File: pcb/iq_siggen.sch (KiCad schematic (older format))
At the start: 130 parts, among them J1 Conn_Coaxial, J10 Conn_01x01_Male, J11 Conn_01x01_Male, J12 Conn_01x01_Male, J13 Conn_01x01_Male, J14 Conn_01x01_Male, J15 Conn_Coaxial, J16 Conn_Coaxial, J17 Conn_01x01_Male, J2 Barrel_Jack_MountingPin, J3 J3 - BANK0, J4 J4 - BANK1, J5 Conn_Coaxial, J6 Conn_Coaxial, J7 Conn_01x10_Male, J8 Conn_01x01_Male, J9 Conn_01x10_Male, SW1 SW_Push, SW2 SW_Push, SW3 SW_Push, SW4 SW_Push, U1 AMS1117-3.3, U2 TPS72325DBVR, U3 TLV73325PDBVT

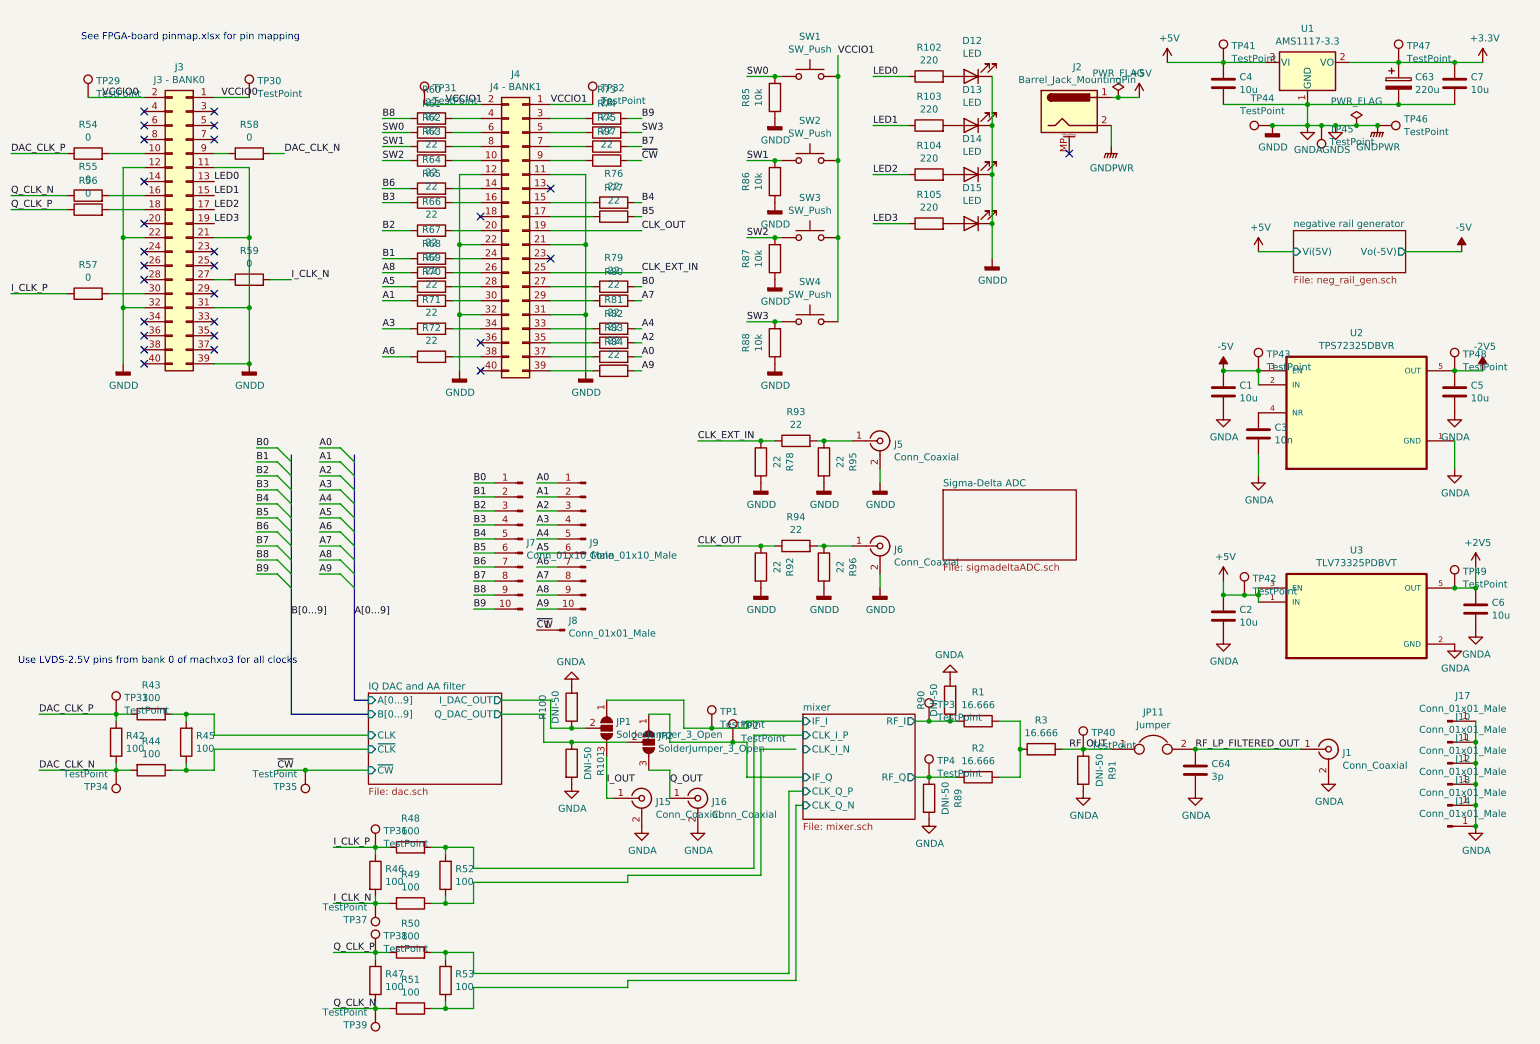
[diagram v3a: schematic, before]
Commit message: Update footprints, move to 0603 passives for JLCPCB assembly, create transformer footprints
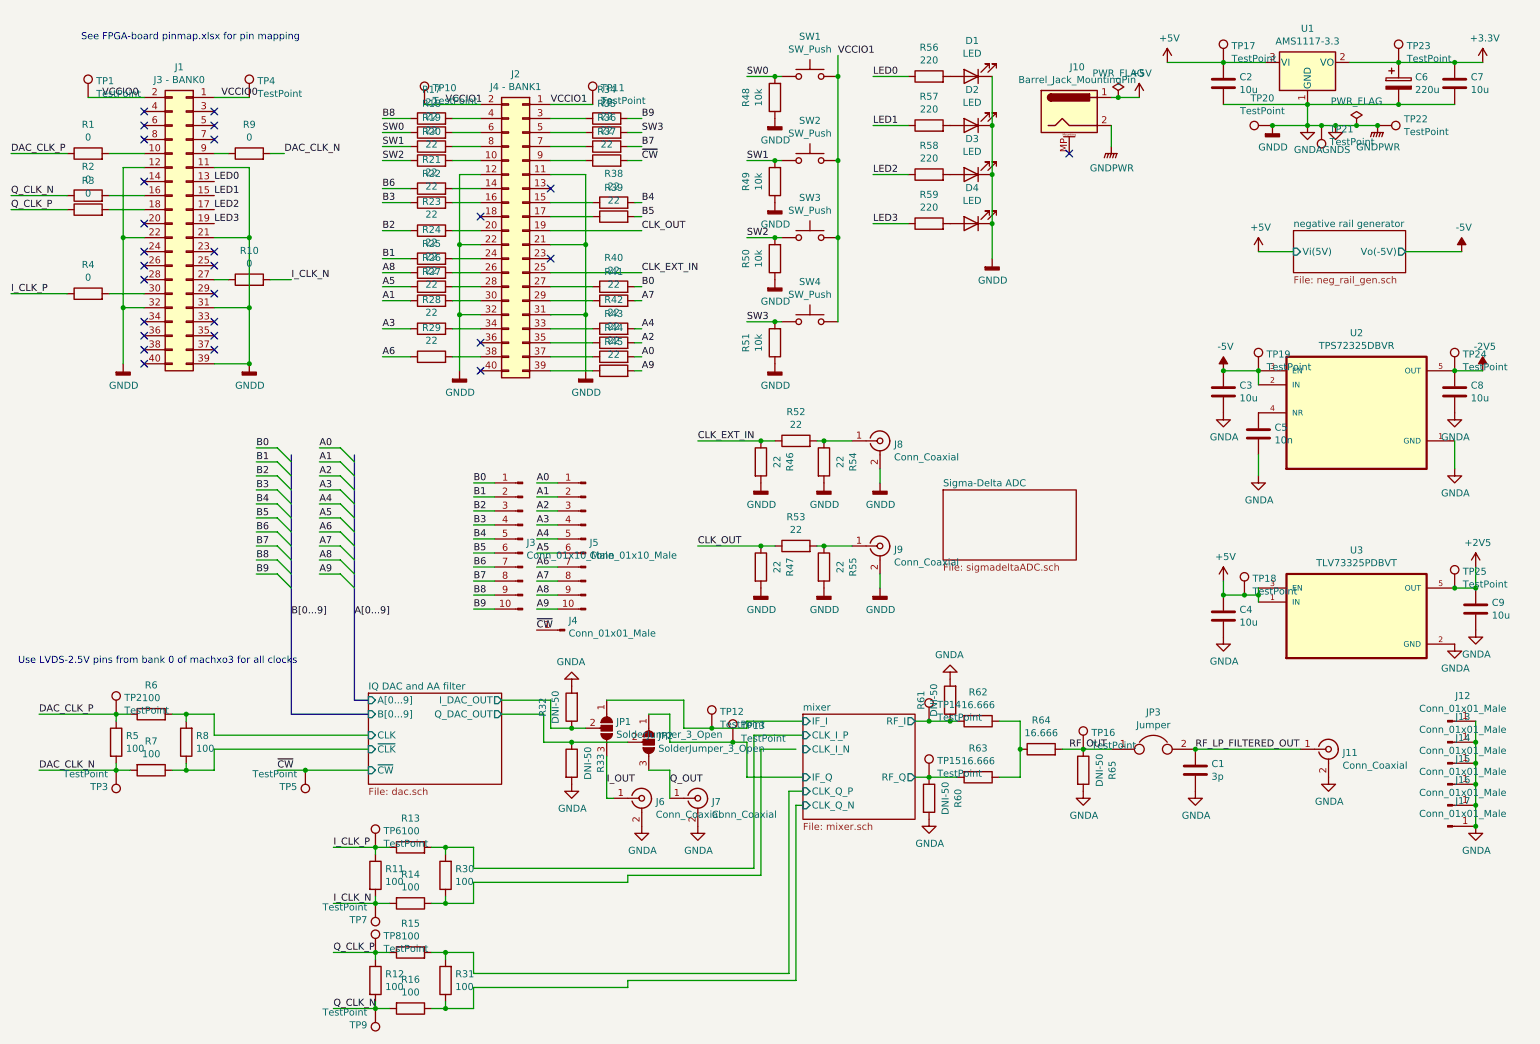
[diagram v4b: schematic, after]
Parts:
- C1: renamed from C64; footprint Capacitor_SMD:C_0805_2012Metric_Pad1.15x1.40mm_HandSolder -> Capacitor_SMD:C_0603_1608Metric
- C2: renamed from C4; footprint Capacitor_SMD:C_0805_2012Metric_Pad1.15x1.40mm_HandSolder -> Capacitor_SMD:C_0603_1608Metric
- C3: renamed from C1; footprint Capacitor_SMD:C_0805_2012Metric_Pad1.15x1.40mm_HandSolder -> Capacitor_SMD:C_0603_1608Metric
- C4: renamed from C2; footprint Capacitor_SMD:C_0805_2012Metric_Pad1.15x1.40mm_HandSolder -> Capacitor_SMD:C_0603_1608Metric
- C5: renamed from C3; footprint Capacitor_SMD:C_0805_2012Metric_Pad1.15x1.40mm_HandSolder -> Capacitor_SMD:C_0603_1608Metric
- C7: footprint Capacitor_SMD:C_0805_2012Metric_Pad1.15x1.40mm_HandSolder -> Capacitor_SMD:C_0603_1608Metric
- C8: renamed from C5; footprint Capacitor_SMD:C_0805_2012Metric_Pad1.15x1.40mm_HandSolder -> Capacitor_SMD:C_0603_1608Metric
- C9: renamed from C6; footprint Capacitor_SMD:C_0805_2012Metric_Pad1.15x1.40mm_HandSolder -> Capacitor_SMD:C_0603_1608Metric
- J1: renamed from J3; footprint (none) -> Connector_PinHeader_2.54mm:PinHeader_2x20_P2.54mm_Vertical
- J11: renamed from J1; footprint (none) -> Connector_Coaxial:SMA_Amphenol_132289_EdgeMount
- J12: renamed from J17; footprint (none) -> Connector_PinHeader_2.54mm:PinHeader_1x01_P2.54mm_Vertical
- J13: renamed from J10; footprint (none) -> Connector_PinHeader_2.54mm:PinHeader_1x01_P2.54mm_Vertical
- J14: renamed from J11; footprint (none) -> Connector_PinHeader_2.54mm:PinHeader_1x01_P2.54mm_Vertical
- J15: renamed from J12; footprint (none) -> Connector_PinHeader_2.54mm:PinHeader_1x01_P2.54mm_Vertical
- J16: renamed from J13; footprint (none) -> Connector_PinHeader_2.54mm:PinHeader_1x01_P2.54mm_Vertical
- J17: renamed from J14; footprint (none) -> Connector_PinHeader_2.54mm:PinHeader_1x01_P2.54mm_Vertical
- J2: renamed from J4; footprint (none) -> Connector_PinHeader_2.54mm:PinHeader_2x20_P2.54mm_Vertical
- J3: renamed from J7; footprint (none) -> Connector_PinHeader_2.54mm:PinHeader_1x10_P2.54mm_Vertical
- J4: renamed from J8; footprint (none) -> Connector_PinHeader_2.54mm:PinHeader_1x01_P2.54mm_Vertical
- J5: renamed from J9; footprint (none) -> Connector_PinHeader_2.54mm:PinHeader_1x10_P2.54mm_Vertical
- J6: renamed from J15; footprint (none) -> Connector_Coaxial:SMA_Amphenol_132289_EdgeMount
- J7: renamed from J16; footprint (none) -> Connector_Coaxial:SMA_Amphenol_132289_EdgeMount
- J8: renamed from J5; footprint (none) -> Connector_Coaxial:SMA_Amphenol_132289_EdgeMount
- J9: renamed from J6; footprint (none) -> Connector_Coaxial:SMA_Amphenol_132289_EdgeMount
- R1: renamed from R54; footprint Resistor_SMD:R_0805_2012Metric_Pad1.20x1.40mm_HandSolder -> Resistor_SMD:R_0603_1608Metric
- R10: renamed from R59; footprint Resistor_SMD:R_0805_2012Metric_Pad1.20x1.40mm_HandSolder -> Resistor_SMD:R_0603_1608Metric
- R11: renamed from R46; footprint Resistor_SMD:R_0805_2012Metric_Pad1.20x1.40mm_HandSolder -> Resistor_SMD:R_0603_1608Metric
- R12: renamed from R47; footprint Resistor_SMD:R_0805_2012Metric_Pad1.20x1.40mm_HandSolder -> Resistor_SMD:R_0603_1608Metric
- R13: renamed from R48; footprint Resistor_SMD:R_0805_2012Metric_Pad1.20x1.40mm_HandSolder -> Resistor_SMD:R_0603_1608Metric
- R14: renamed from R49; footprint Resistor_SMD:R_0805_2012Metric_Pad1.20x1.40mm_HandSolder -> Resistor_SMD:R_0603_1608Metric
- R15: renamed from R50; footprint Resistor_SMD:R_0805_2012Metric_Pad1.20x1.40mm_HandSolder -> Resistor_SMD:R_0603_1608Metric
- R16: renamed from R51; footprint Resistor_SMD:R_0805_2012Metric_Pad1.20x1.40mm_HandSolder -> Resistor_SMD:R_0603_1608Metric
- R17: renamed from R60; footprint Resistor_SMD:R_0805_2012Metric_Pad1.20x1.40mm_HandSolder -> Resistor_SMD:R_0603_1608Metric
- R18: renamed from R61; footprint Resistor_SMD:R_0805_2012Metric_Pad1.20x1.40mm_HandSolder -> Resistor_SMD:R_0603_1608Metric
- R19: renamed from R62; footprint Resistor_SMD:R_0805_2012Metric_Pad1.20x1.40mm_HandSolder -> Resistor_SMD:R_0603_1608Metric
- R2: renamed from R55; footprint Resistor_SMD:R_0805_2012Metric_Pad1.20x1.40mm_HandSolder -> Resistor_SMD:R_0603_1608Metric
- R20: renamed from R63; footprint Resistor_SMD:R_0805_2012Metric_Pad1.20x1.40mm_HandSolder -> Resistor_SMD:R_0603_1608Metric
- R21: renamed from R64; footprint Resistor_SMD:R_0805_2012Metric_Pad1.20x1.40mm_HandSolder -> Resistor_SMD:R_0603_1608Metric
- R22: renamed from R65; footprint Resistor_SMD:R_0805_2012Metric_Pad1.20x1.40mm_HandSolder -> Resistor_SMD:R_0603_1608Metric
- R23: renamed from R66; footprint Resistor_SMD:R_0805_2012Metric_Pad1.20x1.40mm_HandSolder -> Resistor_SMD:R_0603_1608Metric
- R24: renamed from R67; footprint Resistor_SMD:R_0805_2012Metric_Pad1.20x1.40mm_HandSolder -> Resistor_SMD:R_0603_1608Metric
- R25: renamed from R68; footprint Resistor_SMD:R_0805_2012Metric_Pad1.20x1.40mm_HandSolder -> Resistor_SMD:R_0603_1608Metric
- R26: renamed from R69; footprint Resistor_SMD:R_0805_2012Metric_Pad1.20x1.40mm_HandSolder -> Resistor_SMD:R_0603_1608Metric
- R27: renamed from R70; footprint Resistor_SMD:R_0805_2012Metric_Pad1.20x1.40mm_HandSolder -> Resistor_SMD:R_0603_1608Metric
- R28: renamed from R71; footprint Resistor_SMD:R_0805_2012Metric_Pad1.20x1.40mm_HandSolder -> Resistor_SMD:R_0603_1608Metric
- R29: renamed from R72; footprint Resistor_SMD:R_0805_2012Metric_Pad1.20x1.40mm_HandSolder -> Resistor_SMD:R_0603_1608Metric
- R3: renamed from R56; footprint Resistor_SMD:R_0805_2012Metric_Pad1.20x1.40mm_HandSolder -> Resistor_SMD:R_0603_1608Metric
- R30: renamed from R52; footprint Resistor_SMD:R_0805_2012Metric_Pad1.20x1.40mm_HandSolder -> Resistor_SMD:R_0603_1608Metric
- R31: renamed from R53; footprint Resistor_SMD:R_0805_2012Metric_Pad1.20x1.40mm_HandSolder -> Resistor_SMD:R_0603_1608Metric
- R32: renamed from R100; footprint Resistor_SMD:R_0805_2012Metric_Pad1.20x1.40mm_HandSolder -> Resistor_SMD:R_0603_1608Metric
- R33: renamed from R101; footprint Resistor_SMD:R_0805_2012Metric_Pad1.20x1.40mm_HandSolder -> Resistor_SMD:R_0603_1608Metric
- R34: renamed from R73; footprint Resistor_SMD:R_0805_2012Metric_Pad1.20x1.40mm_HandSolder -> Resistor_SMD:R_0603_1608Metric
- R35: renamed from R74; footprint Resistor_SMD:R_0805_2012Metric_Pad1.20x1.40mm_HandSolder -> Resistor_SMD:R_0603_1608Metric
- R36: renamed from R75; footprint Resistor_SMD:R_0805_2012Metric_Pad1.20x1.40mm_HandSolder -> Resistor_SMD:R_0603_1608Metric
- R37: renamed from R97; footprint Resistor_SMD:R_0805_2012Metric_Pad1.20x1.40mm_HandSolder -> Resistor_SMD:R_0603_1608Metric
- R38: renamed from R76; footprint Resistor_SMD:R_0805_2012Metric_Pad1.20x1.40mm_HandSolder -> Resistor_SMD:R_0603_1608Metric
- R39: renamed from R77; footprint Resistor_SMD:R_0805_2012Metric_Pad1.20x1.40mm_HandSolder -> Resistor_SMD:R_0603_1608Metric
- R4: renamed from R57; footprint Resistor_SMD:R_0805_2012Metric_Pad1.20x1.40mm_HandSolder -> Resistor_SMD:R_0603_1608Metric
- R40: renamed from R79; footprint Resistor_SMD:R_0805_2012Metric_Pad1.20x1.40mm_HandSolder -> Resistor_SMD:R_0603_1608Metric
- R41: renamed from R80; footprint Resistor_SMD:R_0805_2012Metric_Pad1.20x1.40mm_HandSolder -> Resistor_SMD:R_0603_1608Metric
- R42: renamed from R81; footprint Resistor_SMD:R_0805_2012Metric_Pad1.20x1.40mm_HandSolder -> Resistor_SMD:R_0603_1608Metric
- R43: renamed from R82; footprint Resistor_SMD:R_0805_2012Metric_Pad1.20x1.40mm_HandSolder -> Resistor_SMD:R_0603_1608Metric
- R44: renamed from R83; footprint Resistor_SMD:R_0805_2012Metric_Pad1.20x1.40mm_HandSolder -> Resistor_SMD:R_0603_1608Metric
- R45: renamed from R84; footprint Resistor_SMD:R_0805_2012Metric_Pad1.20x1.40mm_HandSolder -> Resistor_SMD:R_0603_1608Metric
- R46: renamed from R78; footprint Resistor_SMD:R_0805_2012Metric_Pad1.20x1.40mm_HandSolder -> Resistor_SMD:R_0603_1608Metric
- R47: renamed from R92; footprint Resistor_SMD:R_0805_2012Metric_Pad1.20x1.40mm_HandSolder -> Resistor_SMD:R_0603_1608Metric
- R48: renamed from R85; footprint Resistor_SMD:R_0805_2012Metric_Pad1.20x1.40mm_HandSolder -> Resistor_SMD:R_0603_1608Metric
- R49: renamed from R86; footprint Resistor_SMD:R_0805_2012Metric_Pad1.20x1.40mm_HandSolder -> Resistor_SMD:R_0603_1608Metric
- R5: renamed from R42; footprint Resistor_SMD:R_0805_2012Metric_Pad1.20x1.40mm_HandSolder -> Resistor_SMD:R_0603_1608Metric
- R50: renamed from R87; footprint Resistor_SMD:R_0805_2012Metric_Pad1.20x1.40mm_HandSolder -> Resistor_SMD:R_0603_1608Metric
- R51: renamed from R88; footprint Resistor_SMD:R_0805_2012Metric_Pad1.20x1.40mm_HandSolder -> Resistor_SMD:R_0603_1608Metric
- R52: renamed from R93; footprint Resistor_SMD:R_0805_2012Metric_Pad1.20x1.40mm_HandSolder -> Resistor_SMD:R_0603_1608Metric
- R53: renamed from R94; footprint Resistor_SMD:R_0805_2012Metric_Pad1.20x1.40mm_HandSolder -> Resistor_SMD:R_0603_1608Metric
- R54: renamed from R95; footprint Resistor_SMD:R_0805_2012Metric_Pad1.20x1.40mm_HandSolder -> Resistor_SMD:R_0603_1608Metric
- R55: renamed from R96; footprint Resistor_SMD:R_0805_2012Metric_Pad1.20x1.40mm_HandSolder -> Resistor_SMD:R_0603_1608Metric
- R56: renamed from R102; footprint Resistor_SMD:R_0805_2012Metric_Pad1.20x1.40mm_HandSolder -> Resistor_SMD:R_0603_1608Metric
- R57: renamed from R103; footprint Resistor_SMD:R_0805_2012Metric_Pad1.20x1.40mm_HandSolder -> Resistor_SMD:R_0603_1608Metric
- R58: renamed from R104; footprint Resistor_SMD:R_0805_2012Metric_Pad1.20x1.40mm_HandSolder -> Resistor_SMD:R_0603_1608Metric
- R59: renamed from R105; footprint Resistor_SMD:R_0805_2012Metric_Pad1.20x1.40mm_HandSolder -> Resistor_SMD:R_0603_1608Metric
- R6: renamed from R43; footprint Resistor_SMD:R_0805_2012Metric_Pad1.20x1.40mm_HandSolder -> Resistor_SMD:R_0603_1608Metric
- R60: renamed from R89; footprint Resistor_SMD:R_0805_2012Metric_Pad1.20x1.40mm_HandSolder -> Resistor_SMD:R_0603_1608Metric
- R61: renamed from R90; footprint Resistor_SMD:R_0805_2012Metric_Pad1.20x1.40mm_HandSolder -> Resistor_SMD:R_0603_1608Metric
- R62: renamed from R1; footprint Resistor_SMD:R_0805_2012Metric_Pad1.20x1.40mm_HandSolder -> Resistor_SMD:R_0603_1608Metric
- R63: renamed from R2; footprint Resistor_SMD:R_0805_2012Metric_Pad1.20x1.40mm_HandSolder -> Resistor_SMD:R_0603_1608Metric
- R64: renamed from R3; footprint Resistor_SMD:R_0805_2012Metric_Pad1.20x1.40mm_HandSolder -> Resistor_SMD:R_0603_1608Metric
- R65: renamed from R91; footprint Resistor_SMD:R_0805_2012Metric_Pad1.20x1.40mm_HandSolder -> Resistor_SMD:R_0603_1608Metric
- R7: renamed from R44; footprint Resistor_SMD:R_0805_2012Metric_Pad1.20x1.40mm_HandSolder -> Resistor_SMD:R_0603_1608Metric
- R8: renamed from R45; footprint Resistor_SMD:R_0805_2012Metric_Pad1.20x1.40mm_HandSolder -> Resistor_SMD:R_0603_1608Metric
- R9: renamed from R58; footprint Resistor_SMD:R_0805_2012Metric_Pad1.20x1.40mm_HandSolder -> Resistor_SMD:R_0603_1608Metric
- TP1: renamed from TP29; footprint (none) -> TestPoint:TestPoint_Pad_D1.5mm
- TP10: renamed from TP31; footprint (none) -> TestPoint:TestPoint_Pad_D1.5mm
- TP11: renamed from TP32; footprint (none) -> TestPoint:TestPoint_Pad_D1.5mm
- TP12: renamed from TP1; footprint (none) -> TestPoint:TestPoint_Pad_D1.5mm
- TP13: renamed from TP2; footprint (none) -> TestPoint:TestPoint_Pad_D1.5mm
- TP14: renamed from TP3; footprint (none) -> TestPoint:TestPoint_Pad_D1.5mm
- TP15: renamed from TP4; footprint (none) -> TestPoint:TestPoint_Pad_D1.5mm
- TP16: renamed from TP40; footprint (none) -> TestPoint:TestPoint_Pad_D1.5mm
- TP17: renamed from TP41; footprint (none) -> TestPoint:TestPoint_Pad_D1.5mm
- TP18: renamed from TP42; footprint (none) -> TestPoint:TestPoint_Pad_D1.5mm
- TP19: renamed from TP43; footprint (none) -> TestPoint:TestPoint_Pad_D1.5mm
- TP2: renamed from TP33; footprint (none) -> TestPoint:TestPoint_Pad_D1.5mm
- TP20: renamed from TP44; footprint (none) -> TestPoint:TestPoint_Pad_D1.5mm
- TP21: renamed from TP45; footprint (none) -> TestPoint:TestPoint_Pad_D1.5mm
- TP22: renamed from TP46; footprint (none) -> TestPoint:TestPoint_Pad_D1.5mm
- TP23: renamed from TP47; footprint (none) -> TestPoint:TestPoint_Pad_D1.5mm
- TP24: renamed from TP48; footprint (none) -> TestPoint:TestPoint_Pad_D1.5mm
- TP25: renamed from TP49; footprint (none) -> TestPoint:TestPoint_Pad_D1.5mm
- TP3: renamed from TP34; footprint (none) -> TestPoint:TestPoint_Pad_D1.5mm
- TP4: renamed from TP30; footprint (none) -> TestPoint:TestPoint_Pad_D1.5mm
- TP5: renamed from TP35; footprint (none) -> TestPoint:TestPoint_Pad_D1.5mm
- TP6: renamed from TP36; footprint (none) -> TestPoint:TestPoint_Pad_D1.5mm
- TP7: renamed from TP37; footprint (none) -> TestPoint:TestPoint_Pad_D1.5mm
- TP8: renamed from TP38; footprint (none) -> TestPoint:TestPoint_Pad_D1.5mm
- TP9: renamed from TP39; footprint (none) -> TestPoint:TestPoint_Pad_D1.5mm
- U2, U3: footprint (none) -> Package_TO_SOT_SMD:SOT-23-5_HandSoldering
- renumbered C63 to C6, D12 to D1, D13 to D2, D14 to D3, D15 to D4, J2 to J10, JP11 to JP3

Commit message: layout progress
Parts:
- removed R32, R33: DNI-50, Resistor_SMD:R_0603_1608Metric, symbol Device:R
- removed TP11, TP12, TP13, TP4: TestPoint, TestPoint:TestPoint_Pad_D1.5mm, symbol Connector:TestPoint
- J10: footprint (none) -> Connector_BarrelJack:BarrelJack_Horizontal
- J11, J6, J7, J8, J9: footprint Connector_Coaxial:SMA_Amphenol_132289_EdgeMount -> Connector_Coaxial:SMA_Samtec_SMA-J-P-X-ST-EM1_EdgeMount
- JP1, JP2: footprint (none) -> iq_siggen:50ohm_solder_jumper
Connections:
- net mixer/CLK_I_N: now also R14.1, R30.1
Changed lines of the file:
@@
 $EndSheet
-Wire Wire Line
-	4350 5600 4500 5600
 Wire Wire Line
 	5750 5600 5750 5550
@@
 F 0 "J11" H 10000 5725 50  0000 L CNN
 F 1 "Conn_Coaxial" H 10000 5634 50  0000 L CNN
-F 2 "Connector_Coaxial:SMA_Amphenol_132289_EdgeMount" H 9900 5750 50  0001 C CNN
+F 2 "Connector_Coaxial:SMA_Samtec_SMA-J-P-X-ST-EM1_EdgeMount" H 9900 5750 50  0001 C CNN
 F 3 " ~" H 9900 5750 50  0001 C CNN
 	1    9900 5750
@@
 Wire Wire Line
 	7050 5950 6950 5950
-Wire Wire Line
-	5300 5600 5500 5600
-$Comp
-L Connector:TestPoint TP12
-U 1 1 5FDF24D5
-P 5500 5600
-F 0 "TP12" H 5558 5718 50  0000 L CNN
-F 1 "TestPoint" H 5558 5627 50  0000 L CNN
-F 2 "TestPoint:TestPoint_Pad_D1.5mm" H 5700 5600 50  0001 C CNN
-F 3 "~" H 5700 5600 50  0001 C CNN
-	1    5500 5600
-	1    0    0    -1
-$EndComp
-Connection ~ 5500 5600
-Wire Wire Line
-	5500 5600 5750 5600
-$Comp
-L Connector:TestPoint TP13
-U 1 1 5FDF2A8E
-P 5650 5700
-F 0 "TP13" H 5708 5818 50  0000 L CNN
-F 1 "TestPoint" H 5708 5727 50  0000 L CNN
-F 2 "TestPoint:TestPoint_Pad_D1.5mm" H 5850 5700 50  0001 C CNN
-F 3 "~" H 5850 5700 50  0001 C CNN
-	1    5650 5700
-	1    0    0    -1
-$EndComp
-Connection ~ 5650 5700
-Wire Wire Line
-	5650 5700 5750 5700
 $Comp
 L Device:C C7
@@
 F 0 "J10" H 8107 1517 50  0000 C CNN
 F 1 "Barrel_Jack_MountingPin" H 8107 1426 50  0000 C CNN
-F 2 "" H 8100 1160 50  0001 C CNN
+F 2 "Connector_BarrelJack:BarrelJack_Horizontal" H 8100 1160 50  0001 C CNN
 F 3 "~" H 8100 1160 50  0001 C CNN
 	1    8050 1200
@@
 	5800 5650 5800 6600
 Wire Wire Line
-	6100 5750 5850 5750
+	6150 5750 5850 5750
 Wire Wire Line
 	5850 5750 5850 6650
@@
 F 0 "J8" H 6800 3525 50  0000 L CNN
 F 1 "Conn_Coaxial" H 6800 3434 50  0000 L CNN
-F 2 "Connector_Coaxial:SMA_Amphenol_132289_EdgeMount" H 6700 3550 50  0001 C CNN
+F 2 "Connector_Coaxial:SMA_Samtec_SMA-J-P-X-ST-EM1_EdgeMount" H 6700 3550 50  0001 C CNN
 F 3 " ~" H 6700 3550 50  0001 C CNN
 	1    6700 3550
@@
 F 0 "J9" H 6800 4275 50  0000 L CNN
 F 1 "Conn_Coaxial" H 6800 4184 50  0000 L CNN
-F 2 "Connector_Coaxial:SMA_Amphenol_132289_EdgeMount" H 6700 4300 50  0001 C CNN
+F 2 "Connector_Coaxial:SMA_Samtec_SMA-J-P-X-ST-EM1_EdgeMount" H 6700 4300 50  0001 C CNN
 F 3 " ~" H 6700 4300 50  0001 C CNN
 	1    6700 4300
@@
 VCCIO0
 $Comp
-L Connector:TestPoint TP11
-U 1 1 5FFAD275
-P 4650 1150
-F 0 "TP11" H 4708 1268 50  0000 L CNN
-F 1 "TestPoint" H 4708 1177 50  0000 L CNN
-F 2 "TestPoint:TestPoint_Pad_D1.5mm" H 4850 1150 50  0001 C CNN
-F 3 "~" H 4850 1150 50  0001 C CNN
-	1    4650 1150
-	1    0    0    -1
-$EndComp
-$Comp
-L Connector:TestPoint TP4
-U 1 1 5FF50438
-P 2200 1100
-F 0 "TP4" H 2258 1218 50  0000 L CNN
-F 1 "TestPoint" H 2258 1127 50  0000 L CNN
-F 2 "TestPoint:TestPoint_Pad_D1.5mm" H 2400 1100 50  0001 C CNN
-F 3 "~" H 2400 1100 50  0001 C CNN
-	1    2200 1100
-	1    0    0    -1
-$EndComp
-$Comp
 L power:GNDD #PWR021
 U 1 1 60B48D9B
@@
 F 0 "J6" H 5100 6075 50  0000 L CNN
 F 1 "Conn_Coaxial" H 5100 5984 50  0000 L CNN
-F 2 "Connector_Coaxial:SMA_Amphenol_132289_EdgeMount" H 5000 6100 50  0001 C CNN
+F 2 "Connector_Coaxial:SMA_Samtec_SMA-J-P-X-ST-EM1_EdgeMount" H 5000 6100 50  0001 C CNN
 F 3 " ~" H 5000 6100 50  0001 C CNN
 	1    5000 6100
@@
 F 0 "JP1" V 4704 5668 50  0000 L CNN
 F 1 "SolderJumper_3_Open" V 4795 5668 50  0000 L CNN
-F 2 "" H 4750 5600 50  0001 C CNN
+F 2 "iq_siggen:50ohm_solder_jumper" H 4750 5600 50  0001 C CNN
 F 3 "~" H 4750 5600 50  0001 C CNN
 	1    4750 5600
@@
 F 0 "JP2" V 5004 5768 50  0000 L CNN
 F 1 "SolderJumper_3_Open" V 5095 5768 50  0000 L CNN
-F 2 "" H 5050 5700 50  0001 C CNN
+F 2 "iq_siggen:50ohm_solder_jumper" H 5050 5700 50  0001 C CNN
 F 3 "~" H 5050 5700 50  0001 C CNN
 	1    5050 5700
 	0    1    1    0
 $EndComp
-$Comp
-L Device:R R33
-U 1 1 60D6ED28
-P 4500 5850
-F 0 "R33" V 4707 5850 50  0000 C CNN
-F 1 "DNI-50" V 4616 5850 50  0000 C CNN
-F 2 "Resistor_SMD:R_0603_1608Metric" V 4430 5850 50  0001 C CNN
-F 3 "~" H 4500 5850 50  0001 C CNN
-	1    4500 5850
-	1    0    0    -1
-$EndComp
-Connection ~ 4500 5700
-Wire Wire Line
-	4500 5700 4900 5700
-$Comp
-L power:GNDA #PWR05
-U 1 1 60D6F587
-P 4500 6000
-F 0 "#PWR05" H 4500 5750 50  0001 C CNN
-F 1 "GNDA" H 4505 5827 50  0000 C CNN
-F 2 "" H 4500 6000 50  0001 C CNN
-F 3 "" H 4500 6000 50  0001 C CNN
-	1    4500 6000
-	1    0    0    -1
-$EndComp
-$Comp
-L Device:R R32
-U 1 1 60D7105F
-P 4500 5450
-F 0 "R32" V 4707 5450 50  0000 C CNN
-F 1 "DNI-50" V 4616 5450 50  0000 C CNN
-F 2 "Resistor_SMD:R_0603_1608Metric" V 4430 5450 50  0001 C CNN
-F 3 "~" H 4500 5450 50  0001 C CNN
-	1    4500 5450
-	-1   0    0    1
-$EndComp
-$Comp
-L power:GNDA #PWR04
-U 1 1 60D71065
-P 4500 5300
-F 0 "#PWR04" H 4500 5050 50  0001 C CNN
-F 1 "GNDA" H 4505 5127 50  0000 C CNN
-F 2 "" H 4500 5300 50  0001 C CNN
-F 3 "" H 4500 5300 50  0001 C CNN
-	1    4500 5300
-	-1   0    0    1
-$EndComp
-Connection ~ 4500 5600
-Wire Wire Line
-	4500 5600 4600 5600
 $Comp
 L Connector:Conn_Coaxial J7
@@
 F 0 "J7" H 5500 6075 50  0000 L CNN
 F 1 "Conn_Coaxial" H 5500 5984 50  0000 L CNN
-F 2 "Connector_Coaxial:SMA_Amphenol_132289_EdgeMount" H 5400 6100 50  0001 C CNN
+F 2 "Connector_Coaxial:SMA_Samtec_SMA-J-P-X-ST-EM1_EdgeMount" H 5400 6100 50  0001 C CNN
 F 3 " ~" H 5400 6100 50  0001 C CNN
 	1    5400 6100
@@
 	5200 5500 5200 5700
 Wire Wire Line
-	5200 5700 5650 5700
-Wire Wire Line
 	5050 5500 5200 5500
 $Comp
@@
 Wire Wire Line
 	4300 5500 4300 5700
-Wire Wire Line
-	4300 5700 4500 5700
 Text Label 4750 6000 0    50   ~ 0
 I_OUT
@@
 Text Label 8050 5750 0    50   ~ 0
 RF_OUT
+Wire Wire Line
+	5300 5600 5750 5600
+Wire Wire Line
+	5200 5700 5750 5700
+Wire Wire Line
+	4350 5600 4600 5600
+Wire Wire Line
+	4300 5700 4900 5700
 Wire Bus Line
 	2500 3650 2500 5500

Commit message: Add SMA step model
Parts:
- J6, J7, J8, J9: footprint Connector_Coaxial:SMA_Samtec_SMA-J-P-X-ST-EM1_EdgeMount -> iq_siggen:SMA_Samtec_SMA-J-P-X-ST-EM1_EdgeMount_withSTEP
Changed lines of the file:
@@
 F 0 "J8" H 6800 3525 50  0000 L CNN
 F 1 "Conn_Coaxial" H 6800 3434 50  0000 L CNN
-F 2 "Connector_Coaxial:SMA_Samtec_SMA-J-P-X-ST-EM1_EdgeMount" H 6700 3550 50  0001 C CNN
+F 2 "iq_siggen:SMA_Samtec_SMA-J-P-X-ST-EM1_EdgeMount_withSTEP" H 6700 3550 50  0001 C CNN
 F 3 " ~" H 6700 3550 50  0001 C CNN
 	1    6700 3550
@@
 F 0 "J9" H 6800 4275 50  0000 L CNN
 F 1 "Conn_Coaxial" H 6800 4184 50  0000 L CNN
-F 2 "Connector_Coaxial:SMA_Samtec_SMA-J-P-X-ST-EM1_EdgeMount" H 6700 4300 50  0001 C CNN
+F 2 "iq_siggen:SMA_Samtec_SMA-J-P-X-ST-EM1_EdgeMount_withSTEP" H 6700 4300 50  0001 C CNN
 F 3 " ~" H 6700 4300 50  0001 C CNN
 	1    6700 4300
@@
 F 0 "J6" H 5100 6075 50  0000 L CNN
 F 1 "Conn_Coaxial" H 5100 5984 50  0000 L CNN
-F 2 "Connector_Coaxial:SMA_Samtec_SMA-J-P-X-ST-EM1_EdgeMount" H 5000 6100 50  0001 C CNN
+F 2 "iq_siggen:SMA_Samtec_SMA-J-P-X-ST-EM1_EdgeMount_withSTEP" H 5000 6100 50  0001 C CNN
 F 3 " ~" H 5000 6100 50  0001 C CNN
 	1    5000 6100
@@
 F 0 "J7" H 5500 6075 50  0000 L CNN
 F 1 "Conn_Coaxial" H 5500 5984 50  0000 L CNN
-F 2 "Connector_Coaxial:SMA_Samtec_SMA-J-P-X-ST-EM1_EdgeMount" H 5400 6100 50  0001 C CNN
+F 2 "iq_siggen:SMA_Samtec_SMA-J-P-X-ST-EM1_EdgeMount_withSTEP" H 5400 6100 50  0001 C CNN
 F 3 " ~" H 5400 6100 50  0001 C CNN
 	1    5400 6100
